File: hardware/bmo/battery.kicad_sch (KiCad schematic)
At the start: 11 parts, among them Q1 CSD17571Q2, Q2 CSD17571Q2, U2 BQ29700DSER, U3 MAX17260SETD

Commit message: wip start ltc4412 addition
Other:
- moved on the sheet: Q1
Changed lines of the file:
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@@
 	(wire
 		(pts
-			(xy 190.5 82.55) (xy 191.77 82.55)
+			(xy 189.23 82.55) (xy 191.77 82.55)
 		)
 		(stroke
@@
 	(wire
 		(pts
-			(xy 182.88 77.47) (xy 182.88 72.39)
+			(xy 181.61 77.47) (xy 181.61 72.39)
 		)
 		(stroke
@@
 	(wire
 		(pts
-			(xy 154.94 82.55) (xy 180.34 82.55)
+			(xy 154.94 82.55) (xy 179.07 82.55)
 		)
 		(stroke
@@
 	(wire
 		(pts
-			(xy 182.88 72.39) (xy 187.96 72.39)
+			(xy 181.61 72.39) (xy 187.96 72.39)
 		)
 		(stroke
@@
 	(symbol
 		(lib_id "bmo:CSD17571Q2")
-		(at 185.42 80.01 270)
+		(at 184.15 80.01 270)
 		(unit 1)
 		(body_style 1)
@@
 		(fields_autoplaced yes)
 		(property "Reference" "Q1"
-			(at 185.42 86.36 90)
+			(at 184.15 86.36 90)
 			(show_name no)
 			(do_not_autoplace no)
@@
 		)
 		(property "Value" "CSD17571Q2"
-			(at 185.42 88.9 90)
+			(at 184.15 88.9 90)
 			(show_name no)
 			(do_not_autoplace no)
@@
 		)
 		(property "Footprint" "bmo:TRANS_CSD17571Q2"
-			(at 185.42 80.01 0)
+			(at 184.15 80.01 0)
 			(hide yes)
 			(show_name no)
@@
 		)
 		(property "Datasheet" ""
-			(at 185.42 80.01 0)
+			(at 184.15 80.01 0)
 			(hide yes)
 			(show_name no)
@@
 		)
 		(property "Description" "30-V, N channel NexFET™ power MOSFET, single SON 2 mm x 2 mm, 29 mOhm"
-			(at 185.42 80.01 0)
+			(at 184.15 80.01 0)
 			(hide yes)
 			(show_name no)
@@
 		)
 		(property "MF" "Texas Instruments"
-			(at 185.42 80.01 0)
+			(at 184.15 80.01 0)
 			(hide yes)
 			(show_name no)
@@
 		)
 		(property "MAXIMUM_PACKAGE_HEIGHT" "0.85 mm"
-			(at 185.42 80.01 0)
+			(at 184.15 80.01 0)
 			(hide yes)
 			(show_name no)
@@
 		)
 		(property "Package" "WSON-6 Texas Instruments"
-			(at 185.42 80.01 0)
+			(at 184.15 80.01 0)
 			(hide yes)
 			(show_name no)
@@
 		)
 		(property "Price" "None"
-			(at 185.42 80.01 0)
+			(at 184.15 80.01 0)
 			(hide yes)
 			(show_name no)
@@
 		)
 		(property "Check_prices" "https://www.snapeda.com/parts/CSD17571Q2/Texas+Instruments/view-part/?ref=eda"
-			(at 185.42 80.01 0)
+			(at 184.15 80.01 0)
 			(hide yes)
 			(show_name no)
@@
 		)
 		(property "STANDARD" "Manufacturer Recommendations"
-			(at 185.42 80.01 0)
+			(at 184.15 80.01 0)
 			(hide yes)
 			(show_name no)
@@
 		)
 		(property "PARTREV" "A"
-			(at 185.42 80.01 0)
+			(at 184.15 80.01 0)
 			(hide yes)
 			(show_name no)
@@
 		)
 		(property "SnapEDA_Link" "https://www.snapeda.com/parts/CSD17571Q2/Texas+Instruments/view-part/?ref=snap"
-			(at 185.42 80.01 0)
+			(at 184.15 80.01 0)
 			(hide yes)
 			(show_name no)
@@
 		)
 		(property "MP" "CSD17571Q2"
-			(at 185.42 80.01 0)
+			(at 184.15 80.01 0)
 			(hide yes)
 			(show_name no)
@@
 		)
 		(property "Availability" "In Stock"
-			(at 185.42 80.01 0)
+			(at 184.15 80.01 0)
 			(hide yes)
 			(show_name no)
@@
 		)
 		(property "MANUFACTURER" "Texas Instruments"
-			(at 185.42 80.01 0)
-			(hide yes)
-			(show_name no)
+			(at 184.15 80.01 0)
+			(hide yes)
+			(show_name no)

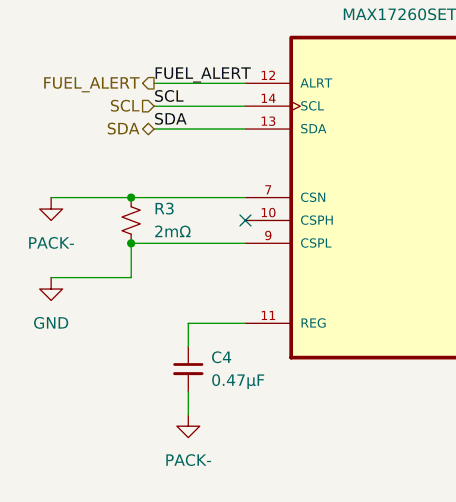
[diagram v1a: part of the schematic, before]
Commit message: Placed and routed everything. DRC is clean.
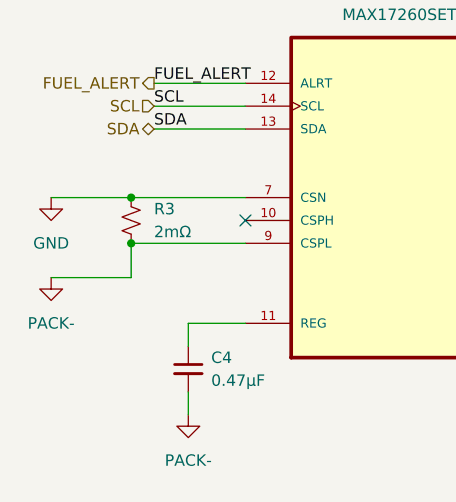
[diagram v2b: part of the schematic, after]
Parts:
- C2, C3, C4: footprint Capacitor_SMD:C_01005_0402Metric -> Capacitor_SMD:C_0402_1005Metric_Pad0.74x0.62mm_HandSolder
- R1, R2: footprint Resistor_SMD:R_01005_0402Metric -> Resistor_SMD:R_0402_1005Metric_Pad0.72x0.64mm_HandSolder
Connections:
- net GND: now also R3.1, U3.7 (CSN); no longer R3.2, U3.9 (CSPL)
- net PACK-: now also R3.2, U3.9 (CSPL); no longer R3.1, U3.7 (CSN)
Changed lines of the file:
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@@
 			)
 		)
-		(property "Footprint" "Capacitor_SMD:C_01005_0402Metric"
+		(property "Footprint" "Capacitor_SMD:C_0402_1005Metric_Pad0.74x0.62mm_HandSolder"
 			(at 120.65 48.26 0)
 			(hide yes)
@@
 				(path "/a1cdc15b-6047-4f5e-b984-2fa9f3f5d7ed/85b2d98d-13b1-41ec-93aa-daec3656f713"
 					(reference "C3")
-					(unit 1)
-				)
-			)
-		)
-	)
-	(symbol
-		(lib_id "power:GND")
-		(at 54.61 69.85 0)
-		(unit 1)
-		(body_style 1)
-		(exclude_from_sim no)
-		(in_bom yes)
-		(on_board yes)
-		(in_pos_files yes)
-		(dnp no)
-		(fields_autoplaced yes)
-		(property "Reference" "#PWR09"
-			(at 54.61 76.2 0)
-			(hide yes)
-			(show_name no)
-			(do_not_autoplace no)
-			(effects
-				(font
-					(size 1.27 1.27)
-				)
-			)
-		)
-		(property "Value" "GND"
-			(at 54.61 74.93 0)
-			(show_name no)
-			(do_not_autoplace no)
-			(effects
-				(font
-					(size 1.27 1.27)
-				)
-			)
-		)
-		(property "Footprint" ""
-			(at 54.61 69.85 0)
-			(hide yes)
-			(show_name no)
-			(do_not_autoplace no)
-			(effects
-				(font
-					(size 1.27 1.27)
-				)
-			)
-		)
-		(property "Datasheet" ""
-			(at 54.61 69.85 0)
-			(hide yes)
-			(show_name no)
-			(do_not_autoplace no)
-			(effects
-				(font
-					(size 1.27 1.27)
-				)
-			)
-		)
-		(property "Description" "Power symbol creates a global label with name \"GND\" , ground"
-			(at 54.61 69.85 0)
-			(hide yes)
-			(show_name no)
-			(do_not_autoplace no)
-			(effects
-				(font
-					(size 1.27 1.27)
-				)
-			)
-		)
-		(pin "1"
-		)
-		(instances
-			(project "bmo"
-				(path "/a1cdc15b-6047-4f5e-b984-2fa9f3f5d7ed/85b2d98d-13b1-41ec-93aa-daec3656f713"
-					(reference "#PWR09")
 					(unit 1)
 				)
@@
 			)
 		)
-		(property "Footprint" "Capacitor_SMD:C_01005_0402Metric"
+		(property "Footprint" "Capacitor_SMD:C_0402_1005Metric_Pad0.74x0.62mm_HandSolder"
 			(at 209.55 53.34 0)
 			(hide yes)
@@
 				(path "/a1cdc15b-6047-4f5e-b984-2fa9f3f5d7ed/85b2d98d-13b1-41ec-93aa-daec3656f713"
 					(reference "C2")
+					(unit 1)
+				)
+			)
+		)
+	)
+	(symbol
+		(lib_id "power:GND")
+		(at 54.61 60.96 0)
+		(unit 1)
+		(body_style 1)
+		(exclude_from_sim no)
+		(in_bom yes)
+		(on_board yes)
+		(in_pos_files yes)
+		(dnp no)
+		(fields_autoplaced yes)
+		(property "Reference" "#PWR09"
+			(at 54.61 67.31 0)
+			(hide yes)
+			(show_name no)
+			(do_not_autoplace no)
+			(effects
+				(font
+					(size 1.27 1.27)
+				)
+			)
+		)
+		(property "Value" "GND"
+			(at 54.61 66.04 0)
+			(show_name no)
+			(do_not_autoplace no)
+			(effects
+				(font
+					(size 1.27 1.27)
+				)
+			)
+		)
+		(property "Footprint" ""
+			(at 54.61 60.96 0)
+			(hide yes)
+			(show_name no)
+			(do_not_autoplace no)
+			(effects
+				(font
+					(size 1.27 1.27)
+				)
+			)
+		)
+		(property "Datasheet" ""
+			(at 54.61 60.96 0)
+			(hide yes)
+			(show_name no)
+			(do_not_autoplace no)
+			(effects
+				(font
+					(size 1.27 1.27)
+				)
+			)
+		)
+		(property "Description" "Power symbol creates a global label with name \"GND\" , ground"
+			(at 54.61 60.96 0)
+			(hide yes)
+			(show_name no)
+			(do_not_autoplace no)
+			(effects
+				(font
+					(size 1.27 1.27)
+				)
+			)
+		)
+		(pin "1"
+		)
+		(instances
+			(project "bmo"
+				(path "/a1cdc15b-6047-4f5e-b984-2fa9f3f5d7ed/85b2d98d-13b1-41ec-93aa-daec3656f713"
+					(reference "#PWR09")
 					(unit 1)
 				)
@@
 	)
 	(symbol
-		(lib_id "power:GND")
-		(at 54.61 60.96 0)
-		(unit 1)
-		(body_style 1)
-		(exclude_from_sim no)
-		(in_bom yes)
-		(on_board yes)
-		(in_pos_files yes)
-		(dnp no)
-		(fields_autoplaced yes)
-		(property "Reference" "#PWR08"
-			(at 54.61 67.31 0)
-			(hide yes)
-			(show_name no)
-			(do_not_autoplace no)
-			(effects
-				(font
-					(size 1.27 1.27)
-				)
-			)
-		)
-		(property "Value" "PACK-"
-			(at 54.61 66.04 0)
-			(show_name no)
-			(do_not_autoplace no)
-			(effects
-				(font
-					(size 1.27 1.27)
-				)
-			)
-		)
-		(property "Footprint" ""
-			(at 54.61 60.96 0)
-			(hide yes)
-			(show_name no)
-			(do_not_autoplace no)
-			(effects
-				(font
-					(size 1.27 1.27)
-				)
-			)
-		)
-		(property "Datasheet" ""
-			(at 54.61 60.96 0)
-			(hide yes)
-			(show_name no)
-			(do_not_autoplace no)
-			(effects
-				(font
-					(size 1.27 1.27)
-				)
-			)
-		)
-		(property "Description" "Power symbol creates a global label with name \"GND\" , ground"
-			(at 54.61 60.96 0)
-			(hide yes)
-			(show_name no)
-			(do_not_autoplace no)
-			(effects
-				(font
-					(size 1.27 1.27)
-				)
-			)
-		)
-		(pin "1"
-		)
-		(instances
-			(project "bmo"
-				(path "/a1cdc15b-6047-4f5e-b984-2fa9f3f5d7ed/85b2d98d-13b1-41ec-93aa-daec3656f713"
-					(reference "#PWR08")
-					(unit 1)
-				)
-			)
-		)
-	)
-	(symbol
 		(lib_id "Device:R_Small_US")
 		(at 63.5 63.5 0)
@@
 			)
 		)
-		(property "Footprint" "Resistor_SMD:R_01005_0402Metric"
+		(property "Footprint" "Resistor_SMD:R_0402_1005Metric_Pad0.72x0.64mm_HandSolder"
 			(at 163.83 58.42 0)
 			(hide yes)
@@
 				(path "/a1cdc15b-6047-4f5e-b984-2fa9f3f5d7ed/85b2d98d-13b1-41ec-93aa-daec3656f713"
 					(reference "R2")
+					(unit 1)
+				)
+			)
+		)
+	)
+	(symbol
+		(lib_id "power:GND")
+		(at 54.61 69.85 0)
+		(unit 1)
+		(body_style 1)
+		(exclude_from_sim no)
+		(in_bom yes)
+		(on_board yes)
+		(in_pos_files yes)
+		(dnp no)
+		(fields_autoplaced yes)
+		(property "Reference" "#PWR08"
+			(at 54.61 76.2 0)
+			(hide yes)
+			(show_name no)
+			(do_not_autoplace no)
+			(effects
+				(font
+					(size 1.27 1.27)
+				)
+			)
+		)
+		(property "Value" "PACK-"
+			(at 54.61 74.93 0)
+			(show_name no)
+			(do_not_autoplace no)
+			(effects
+				(font
+					(size 1.27 1.27)
+				)
+			)
+		)
+		(property "Footprint" ""
+			(at 54.61 69.85 0)
+			(hide yes)
+			(show_name no)
+			(do_not_autoplace no)
+			(effects
+				(font
+					(size 1.27 1.27)
+				)
+			)
+		)
+		(property "Datasheet" ""
+			(at 54.61 69.85 0)
+			(hide yes)
+			(show_name no)
+			(do_not_autoplace no)
+			(effects
+				(font
+					(size 1.27 1.27)
+				)
+			)
+		)
+		(property "Description" "Power symbol creates a global label with name \"GND\" , ground"
+			(at 54.61 69.85 0)
+			(hide yes)
+			(show_name no)
+			(do_not_autoplace no)
+			(effects
+				(font
+					(size 1.27 1.27)
+				)
+			)
+		)
+		(pin "1"
+		)
+		(instances
+			(project "bmo"
+				(path "/a1cdc15b-6047-4f5e-b984-2fa9f3f5d7ed/85b2d98d-13b1-41ec-93aa-daec3656f713"
+					(reference "#PWR08")
 					(unit 1)
 				)
@@
 			)
 		)
-		(property "Footprint" "Capacitor_SMD:C_01005_0402Metric"
+		(property "Footprint" "Capacitor_SMD:C_0402_1005Metric_Pad0.74x0.62mm_HandSolder"
 			(at 69.85 80.01 0)
 			(hide yes)
@@
 			)
 		)
-		(property "Footprint" "Resistor_SMD:R_01005_0402Metric"
+		(property "Footprint" "Resistor_SMD:R_0402_1005Metric_Pad0.72x0.64mm_HandSolder"
 			(at 209.55 44.45 0)
 			(hide yes)
